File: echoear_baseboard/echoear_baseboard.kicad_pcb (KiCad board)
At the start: 2 copper layers, 37.3 x 30.3 mm, 61 parts, among them Q1 AO3401A, Q2 AO3401A, SW1 TS-1088-AR02016, SW2 TS-1088-AR02016, SW3 TS-1088-AR02016, U1 TYPE-C 16PIN 2MD(073), U2 YZ92015035T-04025-01, U3 MountingHole_Pad, U4 A-SP1102DR6GHC-C01-2C, U5 MountingHole_Pad, U6 TLV62569DBV, U7 TP4057, U8 SAM8108

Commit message: First prod draft
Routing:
- net /VBAT: track 10.3 -> 37.1 mm, vias 3 -> 4
- net /VBUS: track 41.4 -> 52.0 mm
- net /MCU_3V3: track 20.0 -> 26.6 mm
- added copper zone on In1.Cu, net GND
- added copper zone on In2.Cu, net GND
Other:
- copper layers 2 -> 4

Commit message: Fixing DRC err part 1
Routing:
- net GND: vias 73 -> 70

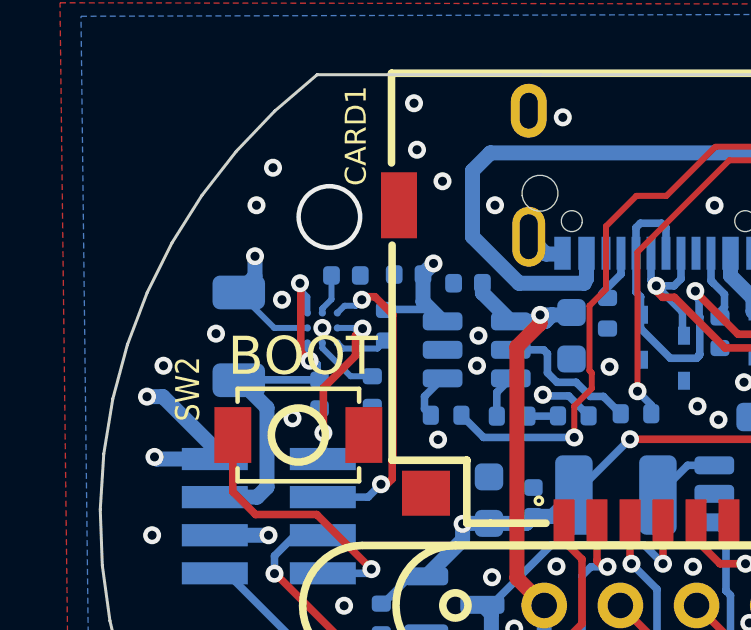
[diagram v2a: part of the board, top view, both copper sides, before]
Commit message: Fixed BQ27220YZFR routing, no more DRC err
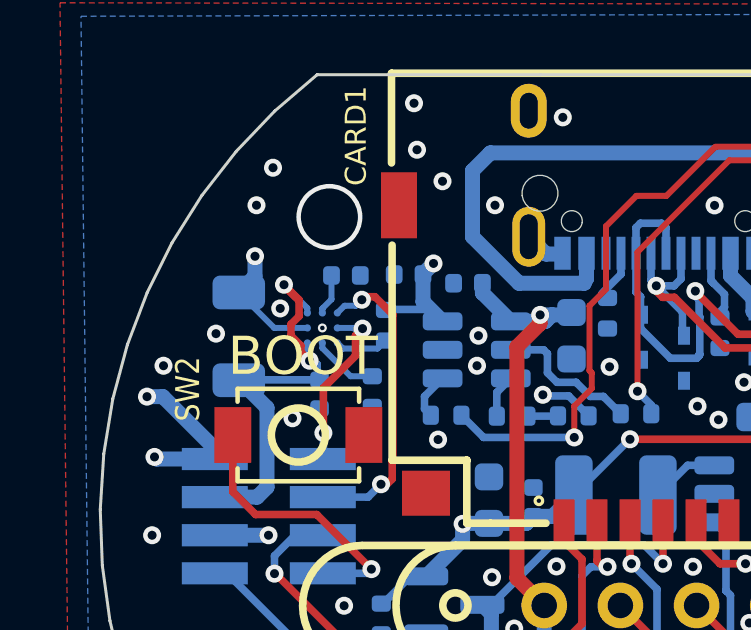
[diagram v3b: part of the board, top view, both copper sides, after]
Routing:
- net /VBAT_IN: track 13.6 -> 15.4 mm
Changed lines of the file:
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@@
 		(capping no)
 		(filling no)
+		(zone_defaults)
 		(pcbplotparams
 			(layerselection 0x00000000_00000000_55555555_5755f5ff)
@@
 		(net "/ESP_RST")
 	)
+	(segment
+		(start 102.595034 66.44)
+		(end 102.626058 66.471024)
+		(width 0.2)
+		(layer "F.Cu")
+		(net "GND")
+	)
 	(via
 		(at 108.990127 76.46)
@@
 		(net "GND")
 	)
+	(via micro
+		(at 102.595034 66.44)
+		(size 0.3)
+		(drill 0.15)
+		(layers "F.Cu" "B.Cu")
+		(net "GND")
+	)
 	(via
 		(at 101.6 69.45)
@@
 	)
 	(via
-		(at 101.25 65.5)
+		(at 101.190421 65.789391)
 		(size 0.6)
 		(drill 0.3)
@@
 	)
 	(via
-		(at 102.595034 66.44)
-		(size 0.6)
-		(drill 0.3)
-		(layers "F.Cu" "B.Cu")
-		(free yes)
-		(net "GND")
-	)
-	(via
 		(at 107.54 81.84)
 		(size 0.6)
@@
 	)
 	(segment
+		(start 102.310661 64.35)
+		(end 106.24 64.35)
+		(width 0.5)
+		(layer "In1.Cu")
+		(net "/VBAT")
+	)
+	(segment
+		(start 102.121322 64.160661)
+		(end 102.310661 64.35)
+		(width 0.5)
+		(layer "In1.Cu")
+		(net "/VBAT")
+	)
+	(segment
 		(start 108.500786 64.29)
 		(end 106.3 64.29)
@@
 	)
 	(segment
-		(start 120.938482 65.635283)
-		(end 120.938482 64.838482)
+		(start 106.24 64.35)
+		(end 106.3 64.29)
 		(width 0.5)
 		(layer "In1.Cu")
@@
 	)
 	(segment
-		(start 100.460661 64.160661)
-		(end 102.121322 64.160661)
+		(start 120.938482 65.635283)
+		(end 120.938482 64.838482)
 		(width 0.5)
 		(layer "In1.Cu")
@@
 	)
 	(segment
-		(start 102.250661 64.29)
-		(end 106.3 64.29)
+		(start 100.460661 64.160661)
+		(end 102.121322 64.160661)
 		(width 0.5)
 		(layer "In1.Cu")
@@
 	)
 	(segment
-		(start 102.121322 64.160661)
-		(end 102.250661 64.29)
-		(width 0.5)
-		(layer "In1.Cu")
-		(net "/VBAT")
-	)
-	(segment
 		(start 117.710786 64.85)
 		(end 117.146929 64.286143)
@@
 	)
 	(segment
-		(start 101.85 64.95)
-		(end 101.877 64.977)
+		(start 101.316005 65.016005)
+		(end 101.724059 65.424059)
 		(width 0.254)
 		(layer "F.Cu")
@@
 	)
 	(segment
-		(start 101.877 64.977)
+		(start 101.877 67.027)
 		(end 101.877 67.240194)
 		(width 0.254)
@@
 	)
 	(segment
+		(start 101.316005 65.028263)
+		(end 101.79779 65.510048)
+		(width 0.254)
+		(layer "F.Cu")
+		(net "/VBAT_IN")
+	)
+	(segment
 		(start 101.877 67.240194)
 		(end 102.169246 67.53244)
@@
 		(net "/VBAT_IN")
 	)
+	(segment
+		(start 101.316005 64.999307)
+		(end 101.817421 65.500723)
+		(width 0.254)
+		(layer "F.Cu")
+		(net "/VBAT_IN")
+	)
+	(segment
+		(start 101.817421 66.049103)
+		(end 101.55 66.316524)
+		(width 0.254)
+		(layer "F.Cu")
+		(net "/VBAT_IN")
+	)
+	(segment
+		(start 101.55 66.7)
+		(end 101.877 67.027)
+		(width 0.254)
+		(layer "F.Cu")
+		(net "/VBAT_IN")
+	)
+	(segment
+		(start 101.316005 64.999307)
+		(end 101.316005 65.016005)
+		(width 0.254)
+		(layer "F.Cu")
+		(net "/VBAT_IN")
+	)
+	(segment
+		(start 101.55 66.316524)
+		(end 101.55 66.7)
+		(width 0.254)
+		(layer "F.Cu")
+		(net "/VBAT_IN")
+	)
+	(segment
+		(start 101.817421 65.500723)
+		(end 101.817421 66.049103)
+		(width 0.254)
+		(layer "F.Cu")
+		(net "/VBAT_IN")
+	)
+	(segment
+		(start 101.316005 64.999307)
+		(end 101.316005 65.028263)
+		(width 0.254)
+		(layer "F.Cu")
+		(net "/VBAT_IN")
+	)
 	(via
 		(at 102.169246 67.53244)
@@
 	)
 	(via
-		(at 101.85 64.95)
+		(at 101.316005 64.999307)
 		(size 0.6)
 		(drill 0.3)
@@
 	)
 	(segment
-		(start 101.85 65.159932)
-		(end 102.095034 65.404966)
-		(width 0.2)
-		(layer "B.Cu")
-		(net "/VBAT_IN")
-	)
-	(segment
-		(start 101.85 64.95)
-		(end 101.85 65.159932)
-		(width 0.2)
-		(layer "B.Cu")
-		(net "/VBAT_IN")
-	)
-	(segment
-		(start 102.095034 65.404966)
-		(end 102.095034 65.94)
+		(start 101.316005 64.999307)
+		(end 102.095034 65.778336)
 		(width 0.2)
 		(layer "B.Cu")
@@
 		(width 0.2)
 		(layer "B.Cu")
+		(net "/VBAT_IN")
+	)
+	(segment
+		(start 102.095034 65.778336)
+		(end 102.095034 65.94)
+		(width 0.2)
+		(layer "B.Cu")

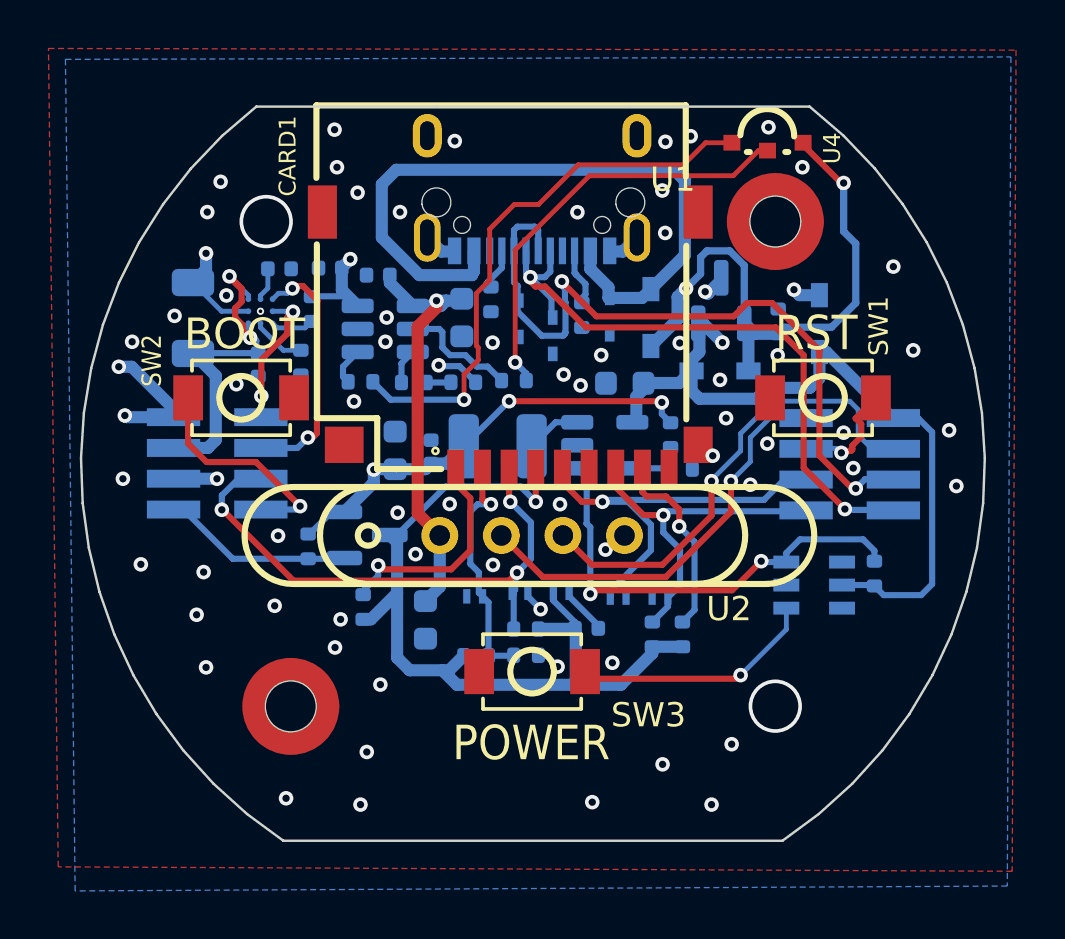
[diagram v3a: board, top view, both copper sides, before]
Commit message: Fixed all possible DRC err
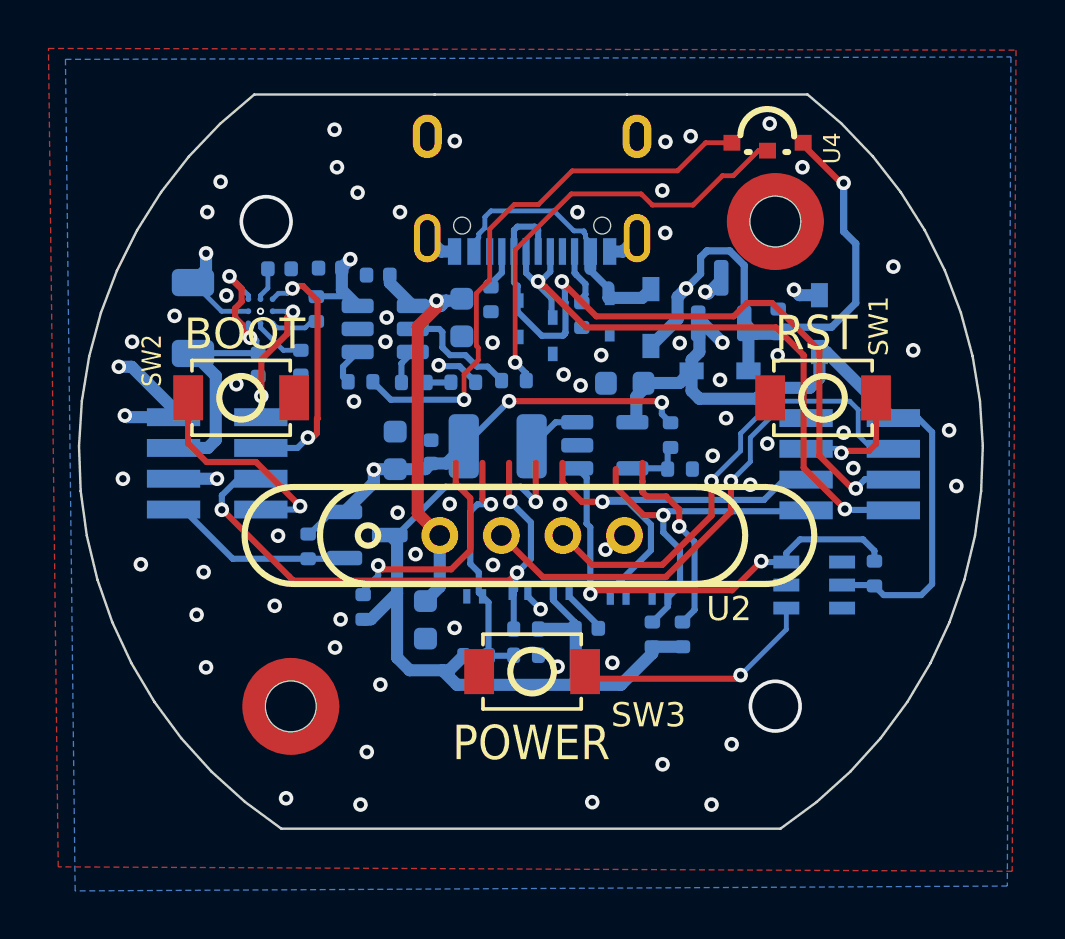
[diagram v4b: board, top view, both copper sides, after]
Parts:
- removed CARD1: HX TF PUSH, Library:TF-SMD_TF-PUSH
- added G***: LOGO, LOGO, B.Cu at (122.6, 60.4)
- U1: moved to B.Cu
- moved G*** 5.64 mm to (104.2, 80.2)
- moved R17 0.20 mm to (104.9, 66.3)
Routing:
- net /VBUS_IN: track 29.7 -> 11.5 mm
- net /VBUS: track 52.0 -> 52.7 mm
- net /USB_DP: track 26.7 -> 26.0 mm
- net GND: vias 70 -> 71
